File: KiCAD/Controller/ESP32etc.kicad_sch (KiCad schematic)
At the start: 6 parts, among them J1 Conn_01x04, J2 Conn_01x04, J3 USB_C_Receptacle_USB2.0_16P, J4 Conn_01x02, J5 Conn_01x02, U2 ESP32_C6_Wroom_1-N8

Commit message: added some parts
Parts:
- added C10: 1u, Capacitor_SMD:C_0603_1608Metric, symbol Device:C
- added C11, C12: 100n, Capacitor_SMD:C_0603_1608Metric, symbol Device:C
- added C9: 100u, Capacitor_SMD:C_1206_3216Metric, symbol Device:C
- added D2: BAT54J, Diode_SMD:D_SOD-323F, symbol Diode:BAT54J
- added R10, R9: 5k, LEDandDriver:R_0603_1608Metric_LedPrj, symbol Device:R
- added R4, R7, R8: 0R, LEDandDriver:R_0603_1608Metric_LedPrj, symbol Device:R
- added R5, R6: 10k, LEDandDriver:R_0603_1608Metric_LedPrj, symbol Device:R
- U2: Manufacturer (none) -> Espressif; Manufacturer Part (none) -> ESP32_C6_Wroom_1-N8; Umax (none) -> 3,3V
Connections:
- net +3.3V: now also J1.1 (Pin_1), C11.1, C9.1, R5.1, R6.1
- net GND: now also J1.4 (Pin_4), J3.A1 (GND), J3.A12 (GND), J3.B1 (GND), J3.B12 (GND), J3.SH (SHIELD), J4.2 (Pin_2), J5.2 (Pin_2), C10.2, C11.2, C12.2, C9.2, R10.1, R9.1
- net PowerGood: now also U2.21 (IO23)
- net at U2.10 (IO8): now also R5.2
- net at U2.13 (IO12): now also R4.1
- net at U2.14 (IO13): now also R7.1
- net at U2.15 (IO9): now also J4.1 (Pin_1)
- net LEDData: now reaches U2.17 (IO19)
- net FanPWM: now reaches U2.19 (IO21)
- net at U2.24 (RXD0): now also J1.3 (Pin_3)
- net at U2.25 (TXD0): now also J1.2 (Pin_2)
- net at U2.3 (EN): now also C10.1, R6.2, R8.2
- net TMS: now reaches U2.4 (IO4)
- net TMS: now also J2.4 (Pin_4)
- net TDI: now reaches U2.5 (IO5)
- net TDI: now also J2.3 (Pin_3)
- net TCK: now reaches U2.6 (IO6)
- net TCK: now also J2.2 (Pin_2)
- net TDO: now reaches U2.7 (IO7)
- net TDO: now also J2.1 (Pin_1)
- net at J3.A4 (VBUS), J3.A9 (VBUS), J3.B4 (VBUS)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: now also D2.2 (A)
- net at J3.A5 (CC1): now also R9.2
- net at J3.A6 (D+), J3.B6 (D+): now also R7.2
- net at J3.A7 (D-), J3.B7 (D-): now also R4.2
- net at J3.B5 (CC2): now also R10.2
- net at J5.1 (Pin_1): now also C12.1, R8.1
- new net +12V: D2.1 (K)
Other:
- moved on the sheet: J1, J2, J4, J5

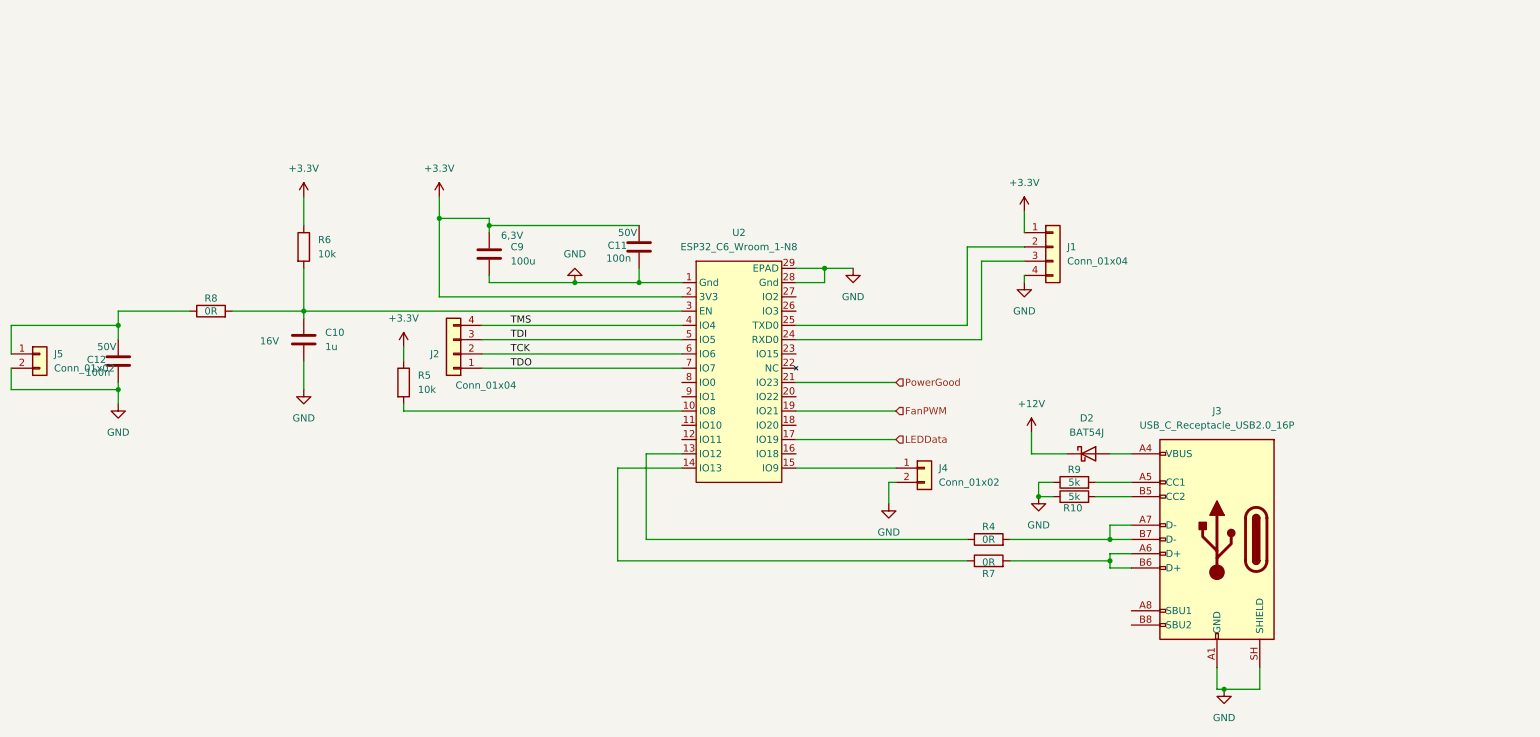
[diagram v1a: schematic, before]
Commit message: switched to original esp footprint and symbol
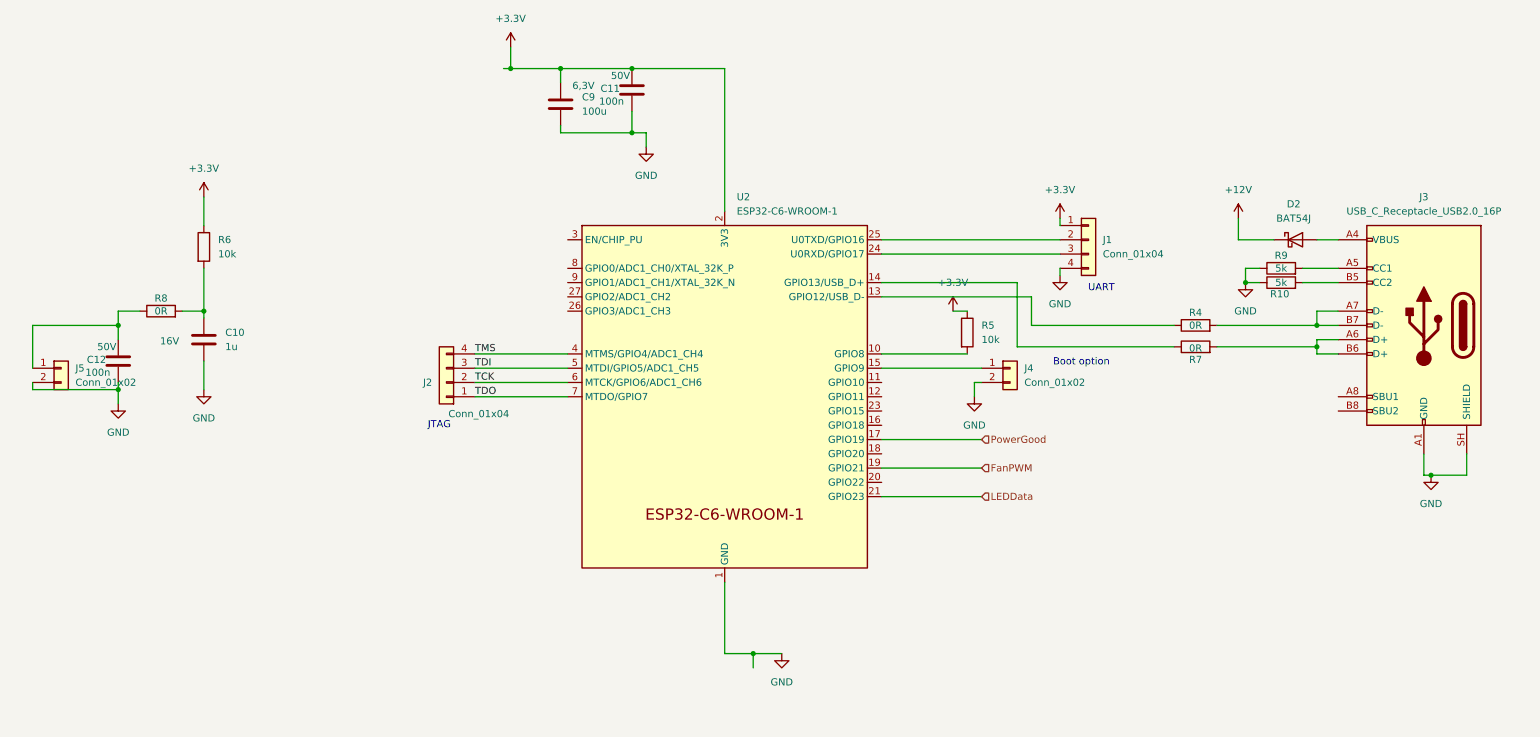
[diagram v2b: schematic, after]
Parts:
- removed U2: ESP32_C6_Wroom_1-N8, LEDandDriver:ESP32-C6-WROOM-1, symbol RGBWW-LED-ProjectLib:ESP32-C6-Wroom-1-N8
- added U2: ESP32-C6-WROOM-1, PCM_Espressif:ESP32-C6-WROOM-1, symbol Espressif:ESP32-C6-WROOM-1
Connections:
- net +3.3V: now also U2.2 (3V3)
- net FanPWM: now also U2.19 (GPIO21)
- net GND: now also U2.1 (GND), U2.28 (GND), U2.29 (GND)
- net LEDData: now also U2.21 (GPIO23)
- net PowerGood: now also U2.17 (GPIO19)
- net TCK: now also U2.6 (MTCK/GPIO6/ADC1_CH6)
- net TDI: now also U2.5 (MTDI/GPIO5/ADC1_CH5)
- net TDO: now also U2.7 (MTDO/GPIO7)
- net TMS: now also U2.4 (MTMS/GPIO4/ADC1_CH4)
- net at R5.2: now also U2.10 (GPIO8)
- net at R4.1: now also U2.13 (GPIO12/USB_D-)
- net at R7.1: now also U2.14 (GPIO13/USB_D+)
- net at J4.1 (Pin_1): now also U2.15 (GPIO9)
- net at J1.3 (Pin_3): now also U2.24 (U0RXD/GPIO17)
- net at J1.2 (Pin_2): now also U2.25 (U0TXD/GPIO16)
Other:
- note added: "Boot option"
- note added: "JTAG"
- note added: "UART"
- moved on the sheet: C10, C11, C9, D2, J1, J2, J3, J4, J5, R10, R4, R5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

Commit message: layout controller finished!
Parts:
- removed J2: Conn_01x04, Connector_PinHeader_2.54mm:PinHeader_1x04_P2.54mm_Vertical_SMD_Pin1Left, symbol Connector_Generic:Conn_01x04
- removed J5: Conn_01x02, Connector_PinHeader_2.54mm:PinHeader_1x02_P2.54mm_Vertical_SMD_Pin1Left, symbol Connector_Generic:Conn_01x02
- added D3: LED, LED_SMD:LED_0603_1608Metric, symbol Device:LED
- added J2: Conn_02x05_Odd_Even, Connector_PinHeader_2.54mm:PinHeader_2x05_P2.54mm_Vertical, symbol Connector_Generic:Conn_02x05_Odd_Even
- added R13: 0R, LEDandDriver:R_0603_1608Metric_LedPrj, symbol Device:R
- added R14: 3k, LEDandDriver:R_0603_1608Metric_LedPrj, symbol Device:R
- added SW1: SW_Push, Button_Switch_THT:SW_PUSH_6mm_H5mm, symbol Switch:SW_Push
- R10, R9: value 5k -> 5k1
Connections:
- net +3.3V: now also J2.1 (Pin_1)
- net GND: now also D3.1 (K), J2.3 (Pin_3), J2.5 (Pin_5), J2.9 (Pin_9), SW1.1
- net TCK: now also J2.4 (Pin_4)
- net TDI: now also J2.8 (Pin_8)
- net TDO: now also J2.6 (Pin_6)
- net TMS: now also J2.2 (Pin_2)
- net at C12.1, R8.1: now also SW1.2
- net D-: now reaches R4.1, U2.13 (GPIO12/USB_D-)
- net D_N: now reaches J3.A7 (D-), J3.B7 (D-), R4.2
- net D+: now reaches R7.1, U2.14 (GPIO13/USB_D+)
- net at U2.20 (GPIO22): now also R14.1
- net at U2.3 (EN/CHIP_PU): now also C10.1, R6.2, R8.2, R13.1
- net D_P: now reaches J3.A6 (D+), J3.B6 (D+), R7.2
- new net: D3.2 (A), R14.2
- new net: J2.10 (Pin_10), R13.2

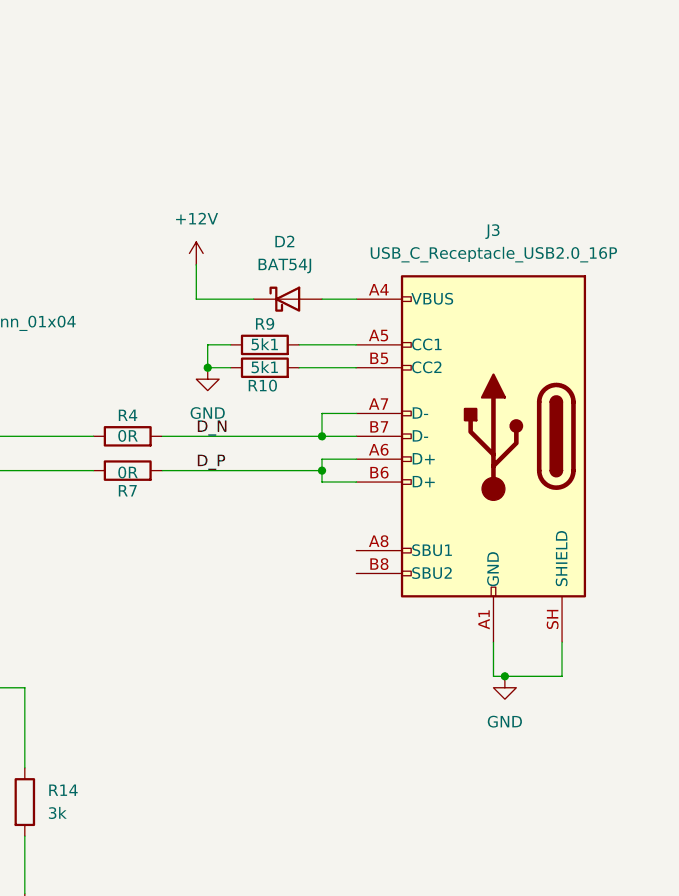
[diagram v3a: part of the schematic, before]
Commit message: longer LED board
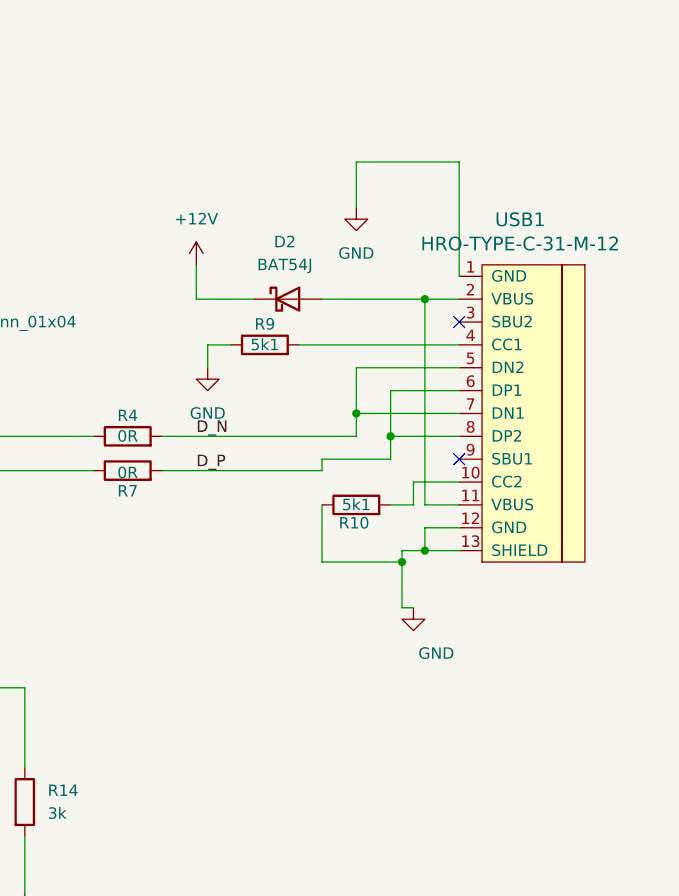
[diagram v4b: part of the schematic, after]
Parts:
- removed J3: USB_C_Receptacle_USB2.0_16P, Connector_USB:USB_C_Receptacle_JAE_DX07S016JA1R1500, symbol Connector:USB_C_Receptacle_USB2.0_16P
- added USB1: HRO-TYPE-C-31-M-12, Type-C:HRO-TYPE-C-31-M-12-Assembly, symbol Type-C:HRO-TYPE-C-31-M-12
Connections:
- net D_N: now also USB1.5 (DN2), USB1.7 (DN1)
- net D_P: now also USB1.6 (DP1), USB1.8 (DP2)
- net GND: now also USB1.1 (GND), USB1.12 (GND), USB1.13 (SHIELD)
- net at D2.2 (A): now also USB1.11 (VBUS), USB1.2 (VBUS)
- net at R9.2: now also USB1.4 (CC1)
- net at R10.2: now also USB1.10 (CC2)
- no-connect marks 0 -> 2
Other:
- moved on the sheet: R10
